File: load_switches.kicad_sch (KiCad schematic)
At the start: 19 parts

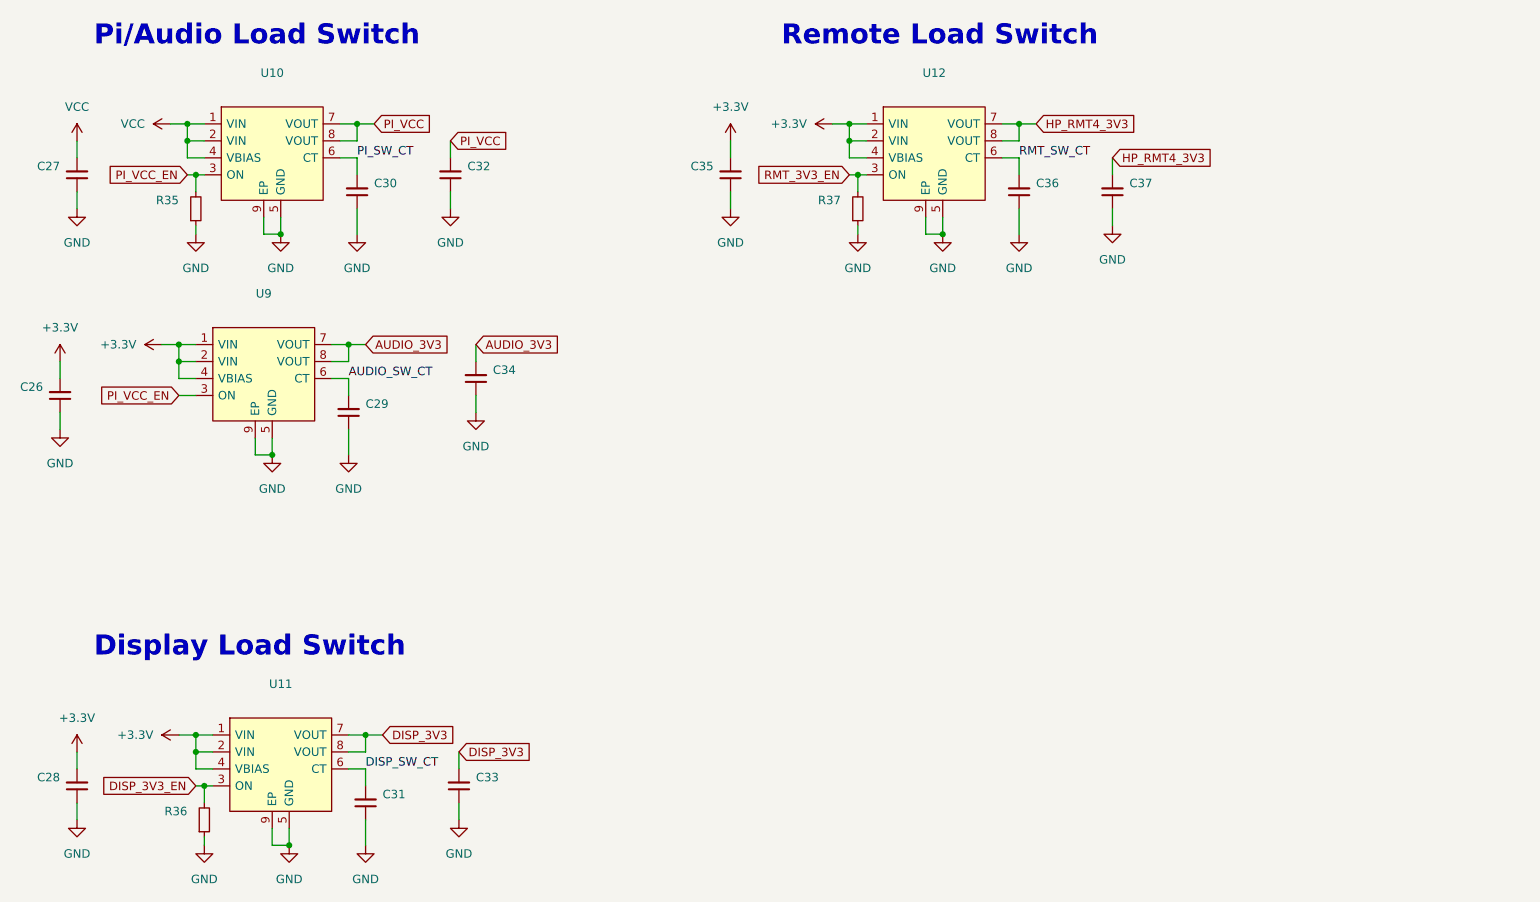
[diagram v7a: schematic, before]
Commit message: layout: add testpoints, extra mounting hole, grounding clips
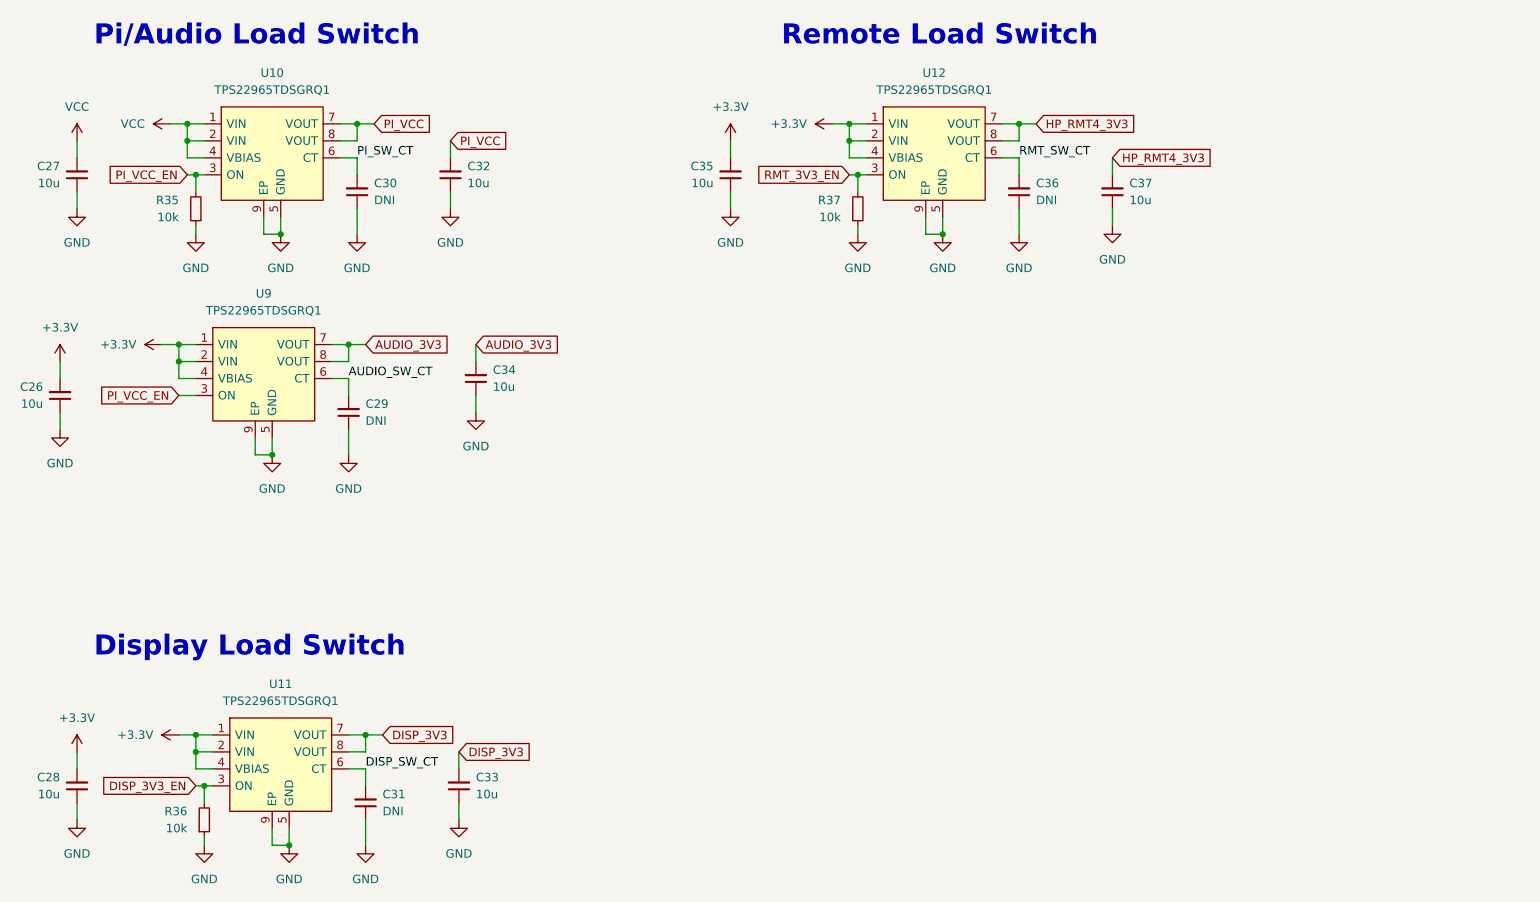
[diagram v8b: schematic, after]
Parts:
- C26, C27, C28, C32, C33, C34, C35, C37: value (none) -> 10u; footprint (none) -> Capacitor_SMD:C_0402_1005Metric
- C29, C30, C31, C36: value (none) -> DNI; footprint (none) -> Capacitor_SMD:C_0402_1005Metric
- R35, R36, R37: value (none) -> 10k; footprint (none) -> Resistor_SMD:R_0402_1005Metric
- U10, U11, U12, U9: value (none) -> TPS22965TDSGRQ1; footprint (none) -> Package_SON:WSON-8-1EP_2x2mm_P0.5mm_EP0.9x1.6mm
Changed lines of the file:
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@@
       (effects (font (size 1.27 1.27)) (justify right))
     )
-    (property "Value" "" (id 1) (at 93.98 78.7335 0)
-      (effects (font (size 1.27 1.27)) (justify right))
-    )
-    (property "Footprint" "" (id 2) (at 91.44 77.47 0)
+    (property "Value" "10u" (id 1) (at 93.98 78.7335 0)
+      (effects (font (size 1.27 1.27)) (justify right))
+    )
+    (property "Footprint" "Capacitor_SMD:C_0402_1005Metric" (id 2) (at 91.44 77.47 0)
       (effects (font (size 1.27 1.27)) hide)
     )
@@
       (effects (font (size 1.27 1.27)) (justify right))
     )
-    (property "Value" "" (id 1) (at 26.67 81.2735 0)
-      (effects (font (size 1.27 1.27)) (justify right))
-    )
-    (property "Footprint" "" (id 2) (at 29.21 80.01 0)
+    (property "Value" "10u" (id 1) (at 26.67 81.2735 0)
+      (effects (font (size 1.27 1.27)) (justify right))
+    )
+    (property "Footprint" "Capacitor_SMD:C_0402_1005Metric" (id 2) (at 29.21 80.01 0)
       (effects (font (size 1.27 1.27)) hide)
     )
@@
       (effects (font (size 1.27 1.27)) (justify right))
     )
-    (property "Value" "" (id 1) (at 76.2 50.7935 0)
-      (effects (font (size 1.27 1.27)) (justify right))
-    )
-    (property "Footprint" "" (id 2) (at 73.66 49.53 0)
+    (property "Value" "DNI" (id 1) (at 76.2 50.7935 0)
+      (effects (font (size 1.27 1.27)) (justify right))
+    )
+    (property "Footprint" "Capacitor_SMD:C_0402_1005Metric" (id 2) (at 73.66 49.53 0)
       (effects (font (size 1.27 1.27)) hide)
     )
@@
       (effects (font (size 1.27 1.27)) (justify right))
     )
-    (property "Value" "" (id 1) (at 77.47 142.2335 0)
-      (effects (font (size 1.27 1.27)) (justify right))
-    )
-    (property "Footprint" "" (id 2) (at 74.93 140.97 0)
+    (property "Value" "DNI" (id 1) (at 77.47 142.2335 0)
+      (effects (font (size 1.27 1.27)) (justify right))
+    )
+    (property "Footprint" "Capacitor_SMD:C_0402_1005Metric" (id 2) (at 74.93 140.97 0)
       (effects (font (size 1.27 1.27)) hide)
     )
@@
       (effects (font (size 1.27 1.27)) (justify right))
     )
-    (property "Value" "" (id 1) (at 91.44 139.6935 0)
-      (effects (font (size 1.27 1.27)) (justify right))
-    )
-    (property "Footprint" "" (id 2) (at 88.9 138.43 0)
+    (property "Value" "10u" (id 1) (at 91.44 139.6935 0)
+      (effects (font (size 1.27 1.27)) (justify right))
+    )
+    (property "Footprint" "Capacitor_SMD:C_0402_1005Metric" (id 2) (at 88.9 138.43 0)
       (effects (font (size 1.27 1.27)) hide)
     )
@@
       (effects (font (size 1.27 1.27)) (justify right))
     )
-    (property "Value" "" (id 1) (at 74.93 83.8135 0)
-      (effects (font (size 1.27 1.27)) (justify right))
-    )
-    (property "Footprint" "" (id 2) (at 72.39 82.55 0)
+    (property "Value" "DNI" (id 1) (at 74.93 83.8135 0)
+      (effects (font (size 1.27 1.27)) (justify right))
+    )
+    (property "Footprint" "Capacitor_SMD:C_0402_1005Metric" (id 2) (at 72.39 82.55 0)
       (effects (font (size 1.27 1.27)) hide)
     )
@@
       (effects (font (size 1.27 1.27)) (justify right))
     )
-    (property "Value" "" (id 1) (at 90.17 48.2535 0)
-      (effects (font (size 1.27 1.27)) (justify right))
-    )
-    (property "Footprint" "" (id 2) (at 87.63 46.99 0)
+    (property "Value" "10u" (id 1) (at 90.17 48.2535 0)
+      (effects (font (size 1.27 1.27)) (justify right))
+    )
+    (property "Footprint" "Capacitor_SMD:C_0402_1005Metric" (id 2) (at 87.63 46.99 0)
       (effects (font (size 1.27 1.27)) hide)
     )
@@
       (effects (font (size 1.27 1.27)) (justify right))
     )
-    (property "Value" "" (id 1) (at 146.05 53.3399 0)
-      (effects (font (size 1.27 1.27)) (justify right))
-    )
-    (property "Footprint" "" (id 2) (at 148.59 52.07 0)
+    (property "Value" "10k" (id 1) (at 146.05 53.3399 0)
+      (effects (font (size 1.27 1.27)) (justify right))
+    )
+    (property "Footprint" "Resistor_SMD:R_0402_1005Metric" (id 2) (at 148.59 52.07 0)
       (effects (font (size 1.27 1.27)) hide)
     )
@@
       (effects (font (size 1.27 1.27)) (justify right))
     )
-    (property "Value" "" (id 1) (at 48.26 144.7799 0)
-      (effects (font (size 1.27 1.27)) (justify right))
-    )
-    (property "Footprint" "" (id 2) (at 50.8 143.51 0)
+    (property "Value" "10k" (id 1) (at 48.26 144.7799 0)
+      (effects (font (size 1.27 1.27)) (justify right))
+    )
+    (property "Footprint" "Resistor_SMD:R_0402_1005Metric" (id 2) (at 50.8 143.51 0)
       (effects (font (size 1.27 1.27)) hide)
     )
@@
       (effects (font (size 1.27 1.27)) (justify right))
     )
-    (property "Value" "" (id 1) (at 46.99 53.3399 0)
-      (effects (font (size 1.27 1.27)) (justify right))
-    )
-    (property "Footprint" "" (id 2) (at 49.53 52.07 0)
+    (property "Value" "10k" (id 1) (at 46.99 53.3399 0)
+      (effects (font (size 1.27 1.27)) (justify right))
+    )
+    (property "Footprint" "Resistor_SMD:R_0402_1005Metric" (id 2) (at 49.53 52.07 0)
       (effects (font (size 1.27 1.27)) hide)
     )
@@
       (effects (font (size 1.27 1.27)) (justify right))
     )
-    (property "Value" "" (id 1) (at 189.23 50.7935 0)
-      (effects (font (size 1.27 1.27)) (justify right))
-    )
-    (property "Footprint" "" (id 2) (at 186.69 49.53 0)
+    (property "Value" "10u" (id 1) (at 189.23 50.7935 0)
+      (effects (font (size 1.27 1.27)) (justify right))
+    )
+    (property "Footprint" "Capacitor_SMD:C_0402_1005Metric" (id 2) (at 186.69 49.53 0)
       (effects (font (size 1.27 1.27)) hide)
     )
@@
       (effects (font (size 1.27 1.27)) (justify right))
     )
-    (property "Value" "" (id 1) (at 29.21 139.6935 0)
-      (effects (font (size 1.27 1.27)) (justify right))
-    )
-    (property "Footprint" "" (id 2) (at 31.75 138.43 0)
+    (property "Value" "10u" (id 1) (at 29.21 139.6935 0)
+      (effects (font (size 1.27 1.27)) (justify right))
+    )
+    (property "Footprint" "Capacitor_SMD:C_0402_1005Metric" (id 2) (at 31.75 138.43 0)
       (effects (font (size 1.27 1.27)) hide)
     )
@@
     (in_bom yes) (on_board yes) (fields_autoplaced)
     (property "Reference" "U10" (id 0) (at 60.96 31.75 0))
-    (property "Value" "" (id 1) (at 60.96 34.29 0))
-    (property "Footprint" "" (id 2) (at 43.18 26.67 0)
+    (property "Value" "TPS22965TDSGRQ1" (id 1) (at 60.96 34.29 0))
+    (property "Footprint" "Package_SON:WSON-8-1EP_2x2mm_P0.5mm_EP0.9x1.6mm" (id 2) (at 43.18 26.67 0)
       (effects (font (size 1.27 1.27)) (justify left) hide)
     )
@@
     (in_bom yes) (on_board yes) (fields_autoplaced)
     (property "Reference" "U12" (id 0) (at 160.02 31.75 0))
-    (property "Value" "" (id 1) (at 160.02 34.29 0))
-    (property "Footprint" "" (id 2) (at 142.24 26.67 0)
+    (property "Value" "TPS22965TDSGRQ1" (id 1) (at 160.02 34.29 0))
+    (property "Footprint" "Package_SON:WSON-8-1EP_2x2mm_P0.5mm_EP0.9x1.6mm" (id 2) (at 142.24 26.67 0)
       (effects (font (size 1.27 1.27)) (justify left) hide)
     )
@@
       (effects (font (size 1.27 1.27)) (justify right))
     )
-    (property "Value" "" (id 1) (at 29.21 48.2535 0)
-      (effects (font (size 1.27 1.27)) (justify right))
-    )
-    (property "Footprint" "" (id 2) (at 31.75 46.99 0)
+    (property "Value" "10u" (id 1) (at 29.21 48.2535 0)
+      (effects (font (size 1.27 1.27)) (justify right))
+    )
+    (property "Footprint" "Capacitor_SMD:C_0402_1005Metric" (id 2) (at 31.75 46.99 0)
       (effects (font (size 1.27 1.27)) hide)
     )
@@
     (in_bom yes) (on_board yes) (fields_autoplaced)
     (property "Reference" "U9" (id 0) (at 59.69 64.77 0))
-    (property "Value" "" (id 1) (at 59.69 67.31 0))
-    (property "Footprint" "" (id 2) (at 41.91 59.69 0)
+    (property "Value" "TPS22965TDSGRQ1" (id 1) (at 59.69 67.31 0))
+    (property "Footprint" "Package_SON:WSON-8-1EP_2x2mm_P0.5mm_EP0.9x1.6mm" (id 2) (at 41.91 59.69 0)
       (effects (font (size 1.27 1.27)) (justify left) hide)
     )
@@
       (effects (font (size 1.27 1.27)) (justify right))
     )
-    (property "Value" "" (id 1) (at 175.26 50.7935 0)
-      (effects (font (size 1.27 1.27)) (justify right))
-    )
-    (property "Footprint" "" (id 2) (at 172.72 49.53 0)
+    (property "Value" "DNI" (id 1) (at 175.26 50.7935 0)
+      (effects (font (size 1.27 1.27)) (justify right))
+    )
+    (property "Footprint" "Capacitor_SMD:C_0402_1005Metric" (id 2) (at 172.72 49.53 0)
       (effects (font (size 1.27 1.27)) hide)
     )
@@
       (effects (font (size 1.27 1.27)) (justify right))
     )
-    (property "Value" "" (id 1) (at 127 48.2535 0)
-      (effects (font (size 1.27 1.27)) (justify right))
-    )
-    (property "Footprint" "" (id 2) (at 129.54 46.99 0)
+    (property "Value" "10u" (id 1) (at 127 48.2535 0)
+      (effects (font (size 1.27 1.27)) (justify right))
+    )
+    (property "Footprint" "Capacitor_SMD:C_0402_1005Metric" (id 2) (at 129.54 46.99 0)
       (effects (font (size 1.27 1.27)) hide)
     )
@@
     (in_bom yes) (on_board yes) (fields_autoplaced)
     (property "Reference" "U11" (id 0) (at 62.23 123.19 0))
-    (property "Value" "" (id 1) (at 62.23 125.73 0))
-    (property "Footprint" "" (id 2) (at 44.45 118.11 0)
-      (effects (font (size 1.27 1.27)) (justify left) hide)
-    )
+    (property "Value" "TPS22965TDSGRQ1" (id 1) (at 62.23 125.73 0))
+    (property "Footprint" "Package_SON:WSON-8-1EP_2x2mm_P0.5mm_EP0.9x1.6mm" (id 2) (at 44.45 118.11 0)
+      (effects (font (size 1.27 1.27)) (justify left) hide)
+    )
